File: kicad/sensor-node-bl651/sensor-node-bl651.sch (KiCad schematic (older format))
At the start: 3 parts

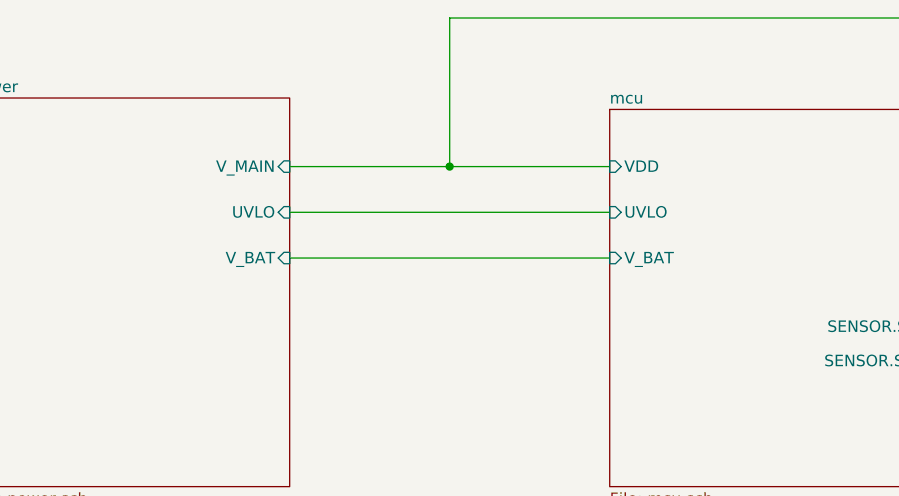
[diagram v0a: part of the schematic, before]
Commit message: add TPS6031x
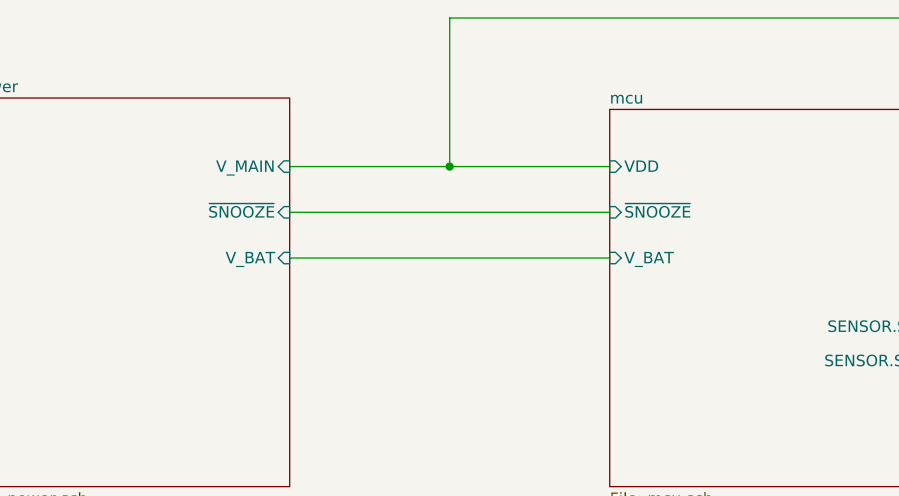
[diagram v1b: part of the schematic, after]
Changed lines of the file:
@@
 F2 "V_MAIN" I R 3050 2350 50
 F3 "V_BAT" I R 3050 2750 50
-F4 "UVLO" I R 3050 2550 50
+F4 "~SNOOZE" I R 3050 2550 50
 $EndSheet
 $Sheet
@@
 F4 "SENSOR.SDA" I R 5900 3200 50
 F5 "V_BAT" I L 4450 2750 50
-F6 "UVLO" I L 4450 2550 50
+F6 "~SNOOZE" I L 4450 2550 50
 $EndSheet
 $Sheet

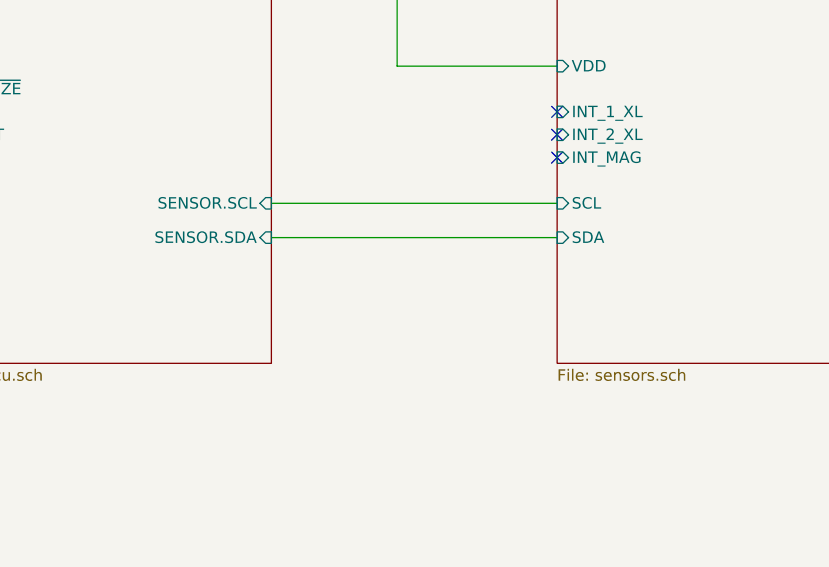
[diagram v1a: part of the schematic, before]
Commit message: add more sensors
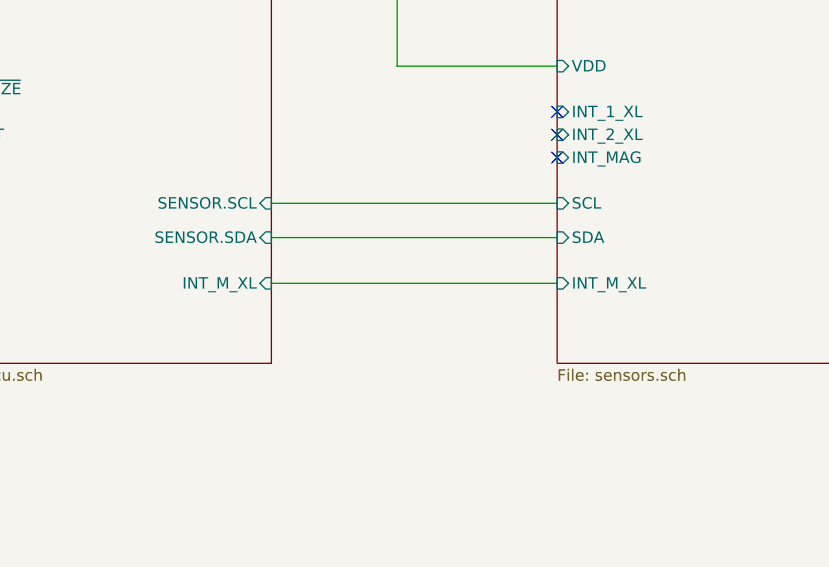
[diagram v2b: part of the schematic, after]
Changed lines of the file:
@@
 F5 "V_BAT" I L 4450 2750 50
 F6 "~SNOOZE" I L 4450 2550 50
+F7 "INT_M_XL" I R 5900 3400 50
 $EndSheet
 $Sheet
@@
 F6 "INT_2_XL" I L 7150 2750 50
 F7 "INT_MAG" I L 7150 2850 50
+F8 "INT_M_XL" I L 7150 3400 50
 $EndSheet
 Wire Wire Line
@@
 Wire Wire Line
 	3050 2550 4450 2550
+Wire Wire Line
+	5900 3400 7150 3400
 $EndSCHEMATC

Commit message: add fuses
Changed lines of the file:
@@
 F2 "V_MAIN" I R 3050 2350 50
 F3 "V_BAT" I R 3050 2750 50
-F4 "~SNOOZE" I R 3050 2550 50
 $EndSheet
 $Sheet
@@
 F4 "SENSOR.SDA" I R 5900 3200 50
 F5 "V_BAT" I L 4450 2750 50
-F6 "~SNOOZE" I L 4450 2550 50
-F7 "INT_M_XL" I R 5900 3400 50
+F6 "INT_M_XL" I R 5900 3400 50
 $EndSheet
 $Sheet
@@
 NoConn ~ 7150 2850
 Wire Wire Line
-	3050 2550 4450 2550
-Wire Wire Line
 	5900 3400 7150 3400

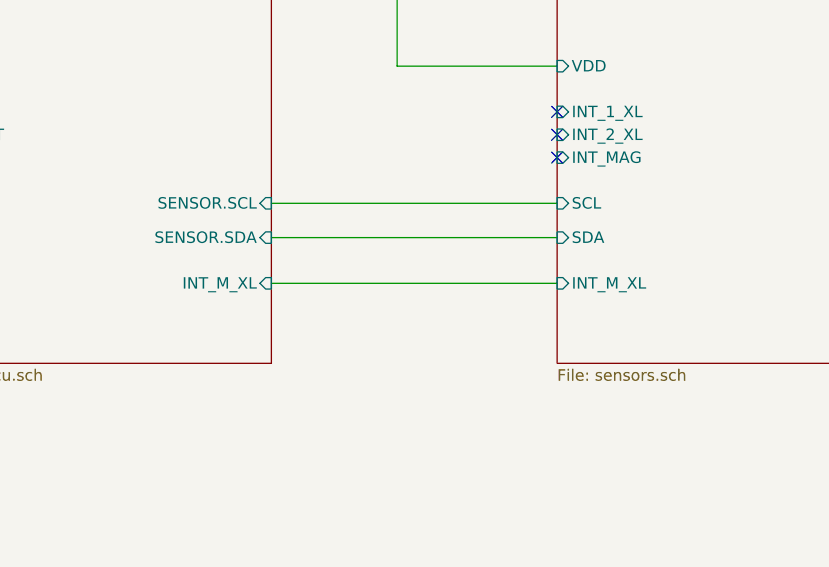
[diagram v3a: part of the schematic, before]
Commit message: remove memsic sensors
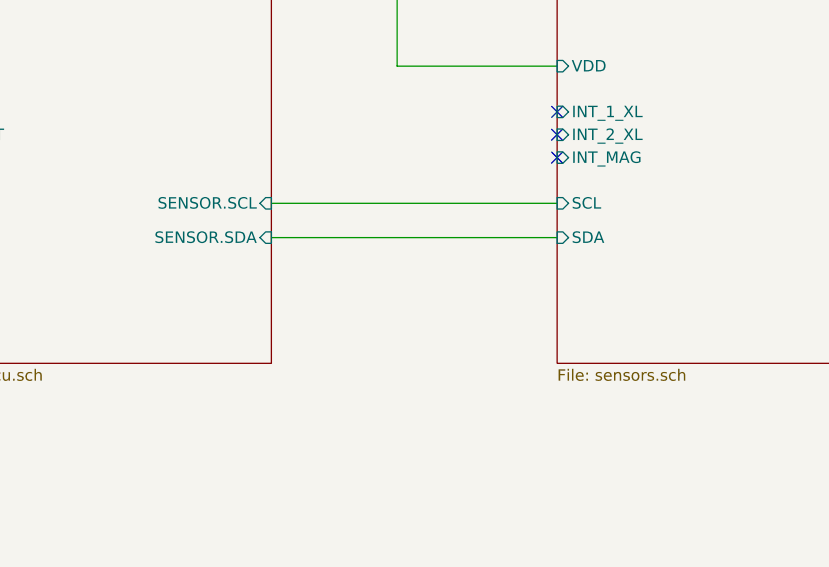
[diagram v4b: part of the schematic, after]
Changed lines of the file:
@@
 F4 "SENSOR.SDA" I R 5900 3200 50
 F5 "V_BAT" I L 4450 2750 50
-F6 "INT_M_XL" I R 5900 3400 50
-$EndSheet
-$Sheet
-S 7150 2100 1650 1650
-U 6016C959
-F0 "sensors" 50
-F1 "sensors.sch" 50
-F2 "VDD" I L 7150 2450 50
-F3 "SCL" I L 7150 3050 50
-F4 "SDA" I L 7150 3200 50
-F5 "INT_1_XL" I L 7150 2650 50
-F6 "INT_2_XL" I L 7150 2750 50
-F7 "INT_MAG" I L 7150 2850 50
-F8 "INT_M_XL" I L 7150 3400 50
 $EndSheet
 Wire Wire Line
@@
 NoConn ~ 7150 2750
 NoConn ~ 7150 2850
-Wire Wire Line
-	5900 3400 7150 3400
+$Sheet
+S 7150 2100 1650 1650
+U 6016C959
+F0 "sensors" 50
+F1 "sensors.sch" 50
+F2 "VDD" I L 7150 2450 50
+F3 "SCL" I L 7150 3050 50
+F4 "SDA" I L 7150 3200 50
+F5 "INT_1_XL" I L 7150 2650 50
+F6 "INT_2_XL" I L 7150 2750 50
+F7 "INT_MAG" I L 7150 2850 50
+$EndSheet
 $EndSCHEMATC
